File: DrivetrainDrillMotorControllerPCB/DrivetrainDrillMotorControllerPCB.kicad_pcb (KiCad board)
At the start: 4 copper layers, 100 x 100 mm, 39 parts, among them J1 DC-005-5A-2.0, J10 Conn_01x02_Socket, J11 Conn_01x02_Socket, J12 Conn_01x02_Socket, J13 Conn_01x02_Socket, J14 Conn_01x02_Socket, J15 Conn_01x02_Socket, J16 Conn_01x02_Socket, J17 Conn_01x08_Socket, J2 Conn_01x02_Socket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

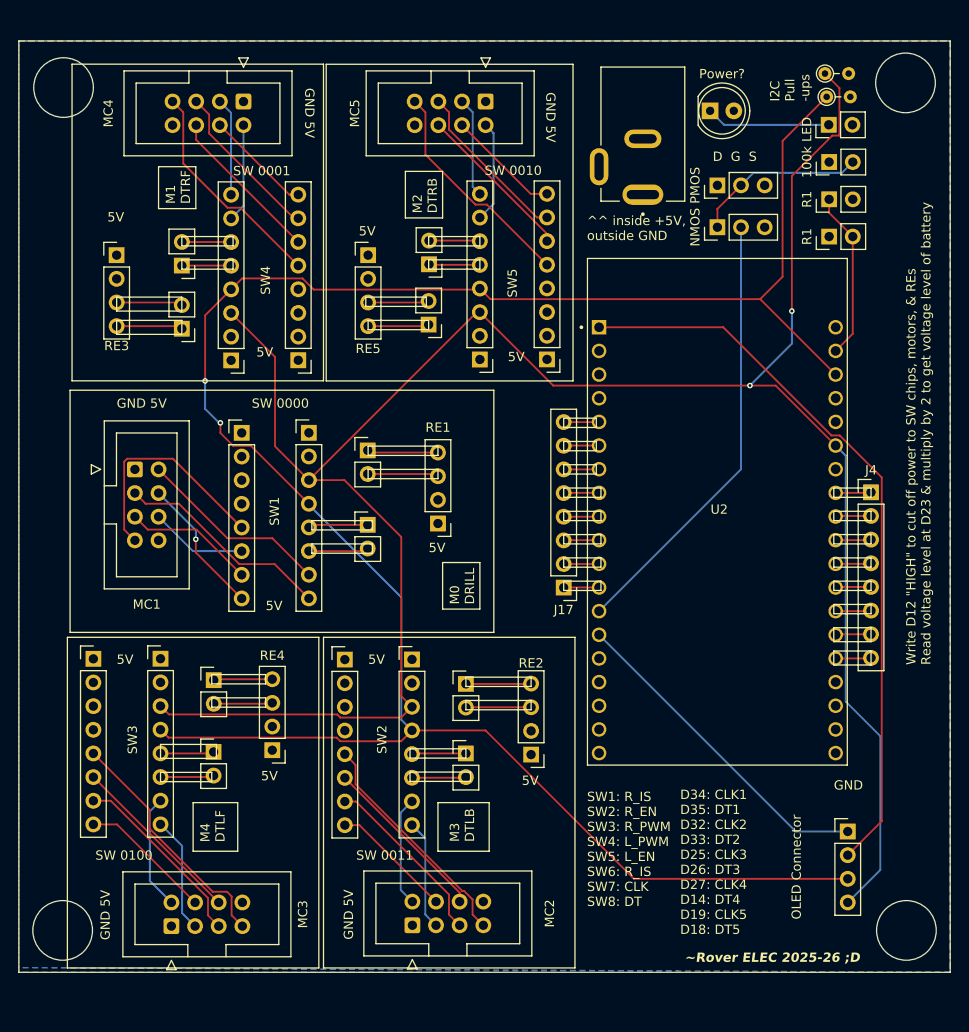
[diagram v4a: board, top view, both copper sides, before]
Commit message: Corrected devkit footprint
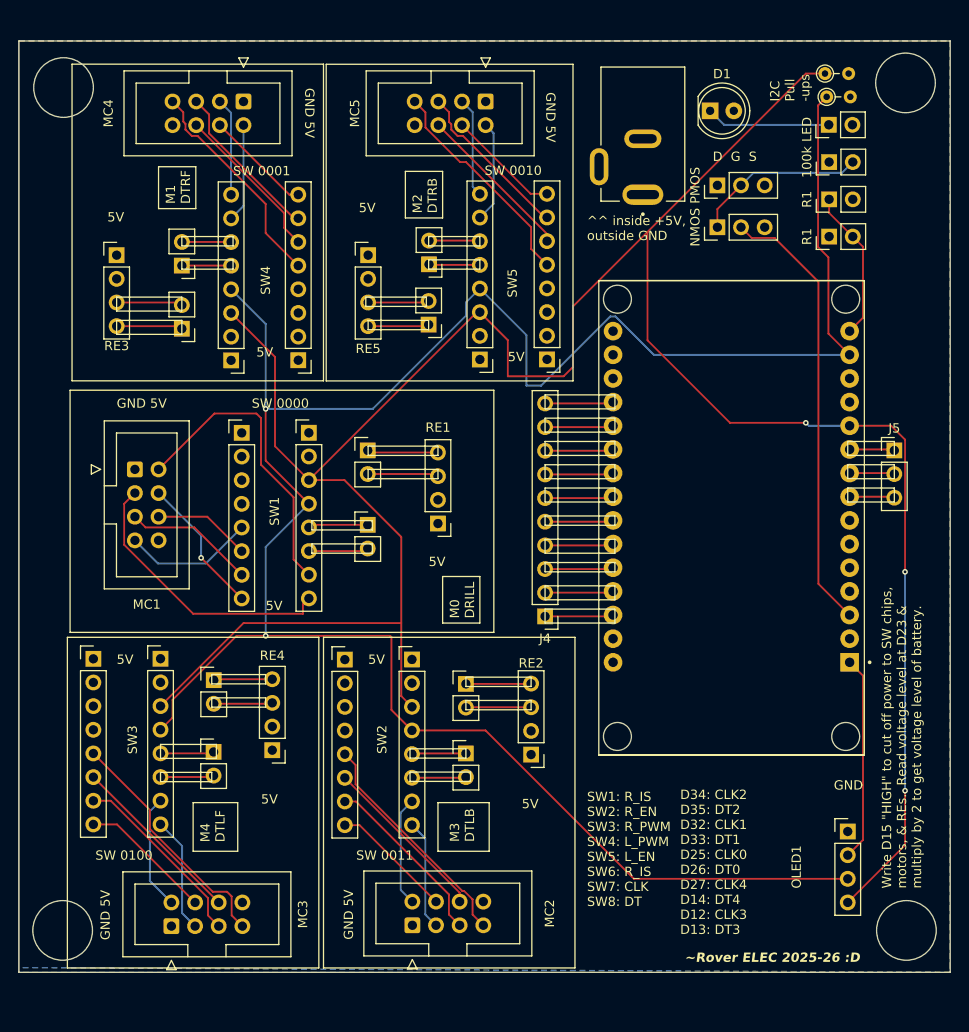
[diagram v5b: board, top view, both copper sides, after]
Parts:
- removed J17: Conn_01x08_Socket, Connector_PinHeader_2.54mm:PinHeader_1x08_P2.54mm_Vertical
- removed U2: ESP32-DEVKITC-32D, ESP32-DEVKITC-32D:MODULE_ESP32-DEVKITC-32D
- added J5: Conn_01x03_Socket, Connector_PinHeader_2.54mm:PinHeader_1x03_P2.54mm_Vertical, F.Cu at (151.5, 104.0)
- added U1: ESP32-DEVKIT-V1, ESP32-DEVKIT-V1:MODULE_ESP32_DEVKIT_V1, F.Cu at (134.0, 111.2)
- J4: value Conn_01x08_Socket -> Conn_01x10_Socket; footprint Connector_PinHeader_2.54mm:PinHeader_1x08_P2.54mm_Vertical -> Connector_PinHeader_2.54mm:PinHeader_1x10_P2.54mm_Vertical
- OLED1: renamed from OLED Connector
- moved J4 37.4 mm to (114.0, 121.8), turned to 180 degrees
- gave numbers to parts that had none: 1
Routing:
- net 3.3V: track 79.1 -> 22.0 mm
- net GND: track 35.4 -> 0.00 mm
- net SDA: track 241.6 -> 264.0 mm, vias 2 -> 3
- net SCL: track 234.7 -> 248.0 mm
- net Net-(MC1-Pin_2): track 20.8 -> 32.6 mm
- net Net-(MC1-Pin_7): track 24.7 -> 14.1 mm
- net Net-(J4-Pin_9): track 0.00 -> 7.36 mm
- net Net-(J4-Pin_10): track 0.00 -> 7.36 mm
- net Net-(MC1-Pin_3): track 23.4 -> 30.2 mm
- net Net-(J5-Pin_3): track 0.00 -> 4.84 mm
- net Net-(J5-Pin_2): track 0.00 -> 4.84 mm
- net Net-(J5-Pin_1): track 0.00 -> 4.84 mm
- net Net-(J17-Pin_5): track 3.81 -> 0.00 mm
- net Net-(J17-Pin_3): track 3.81 -> 0.00 mm
- net Net-(J17-Pin_8): track 3.81 -> 0.00 mm
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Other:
- board text added: "D34: CLK2 D35: DT2 D32: CLK1 D33: DT1 D25: CLK0 D26: DT0 D27: CLK4 D14: DT4 D12: CLK3 D13: DT3"
- board text added: "Write D15 {dblquote}HIGH{dblquote} to cut off power to SW chips, motors, & REs. Read voltage level at D23 & multiply by 2 to get voltage level of battery."
- board text added: "~Rover ELEC 2025-26 :D"
- board text removed: "D34: CLK1 D35: DT1 D32: CLK2 D33: DT2 D25: CLK3 D26: DT3 D27: CLK4 D14: DT4 D19: CLK5 D18: DT5"
- board text removed: "Write D12 {dblquote}HIGH{dblquote} to cut off power to SW chips, motors, & REs Read voltage level at D23 & multiply by 2 to get voltage level of battery"
- board text removed: "~Rover ELEC 2025-26 ;D"

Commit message: made esp32 power from battery optional
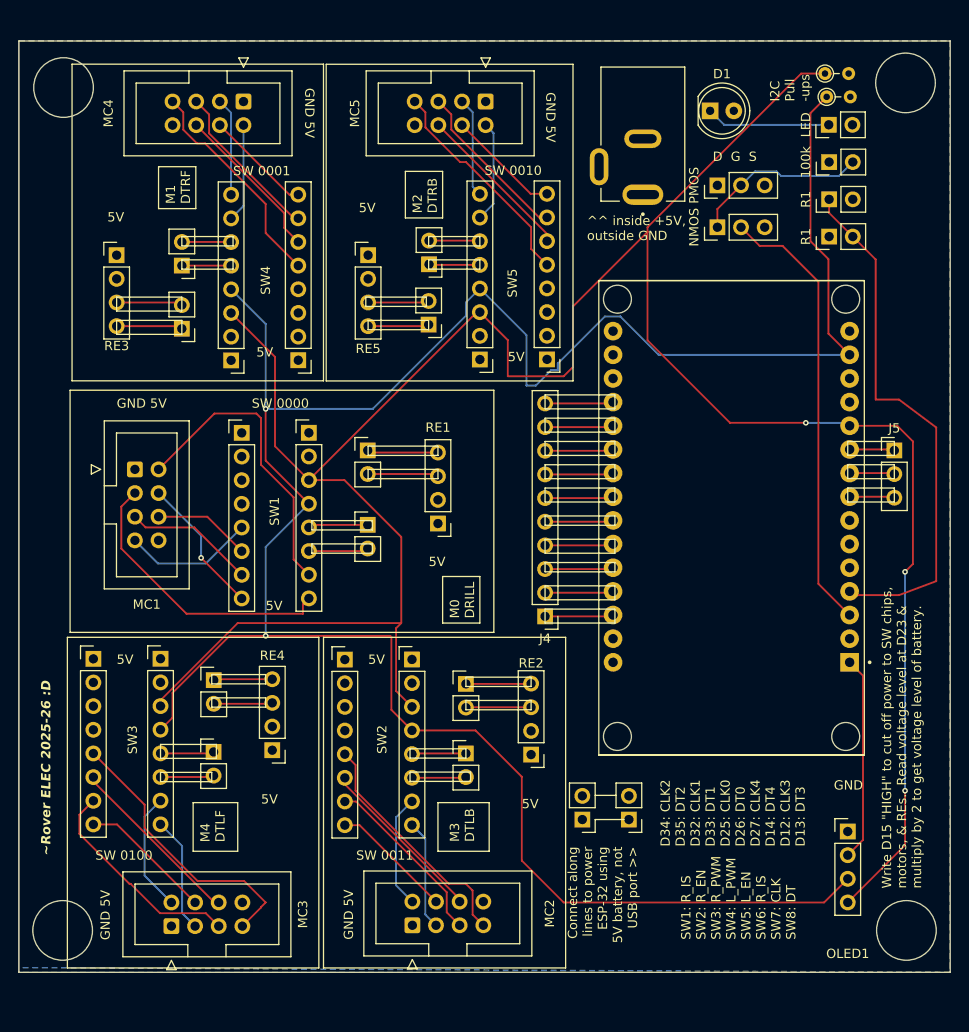
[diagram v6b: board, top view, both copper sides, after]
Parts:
- added J6: Conn_01x02_Socket, Connector_PinHeader_2.54mm:PinHeader_1x02_P2.54mm_Vertical, F.Cu at (123.0, 143.6)
- added J7: Conn_01x02_Socket, Connector_PinHeader_2.54mm:PinHeader_1x02_P2.54mm_Vertical, F.Cu at (118.0, 143.6)
- renumbered 100k to 100k1, PMOS to Q1, NMOS to Q2, R1 to R3, R1 to R4, LED to R5
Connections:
- R3 pad 1: Net-(U1-D23) -> Net-(U1-D2)
- R4 pad 2: Net-(U1-D23) -> Net-(U1-D2)
- U1 pad 15: Net-(U1-D23) -> unconnected-(U1-D23-Pad15)
- U1 pad 30: original5V -> ESP32Feeder
- U1 pad 4: unconnected-(U1-D2-Pad4) -> Net-(U1-D2)
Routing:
- net Net-(U1-D2): track 0.00 -> 23.6 mm
- net Net-(U1-D23): track 16.3 -> 0.00 mm
- net SCL: track 248.0 -> 256.9 mm
- net Net-(MC3-Pin_7): track 26.1 -> 30.2 mm
- net Net-(MC3-Pin_5): track 20.1 -> 23.2 mm
- net SDA: track 264.0 -> 266.3 mm
- net Net-(MC2-Pin_7): track 24.6 -> 25.6 mm
- net Net-(MC1-Pin_3): track 30.2 -> 30.9 mm
- added copper zone on In2.Cu, net ESP32Feeder
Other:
- board text added: "100k"
- board text added: "Connect along lines to power ESP-32 using 5V battery, not USB port >>"
- board text added: "LED"
- board text added: "NMOS"
- board text added: "PMOS"
- board text added: "R1"

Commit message: Added linear regulator
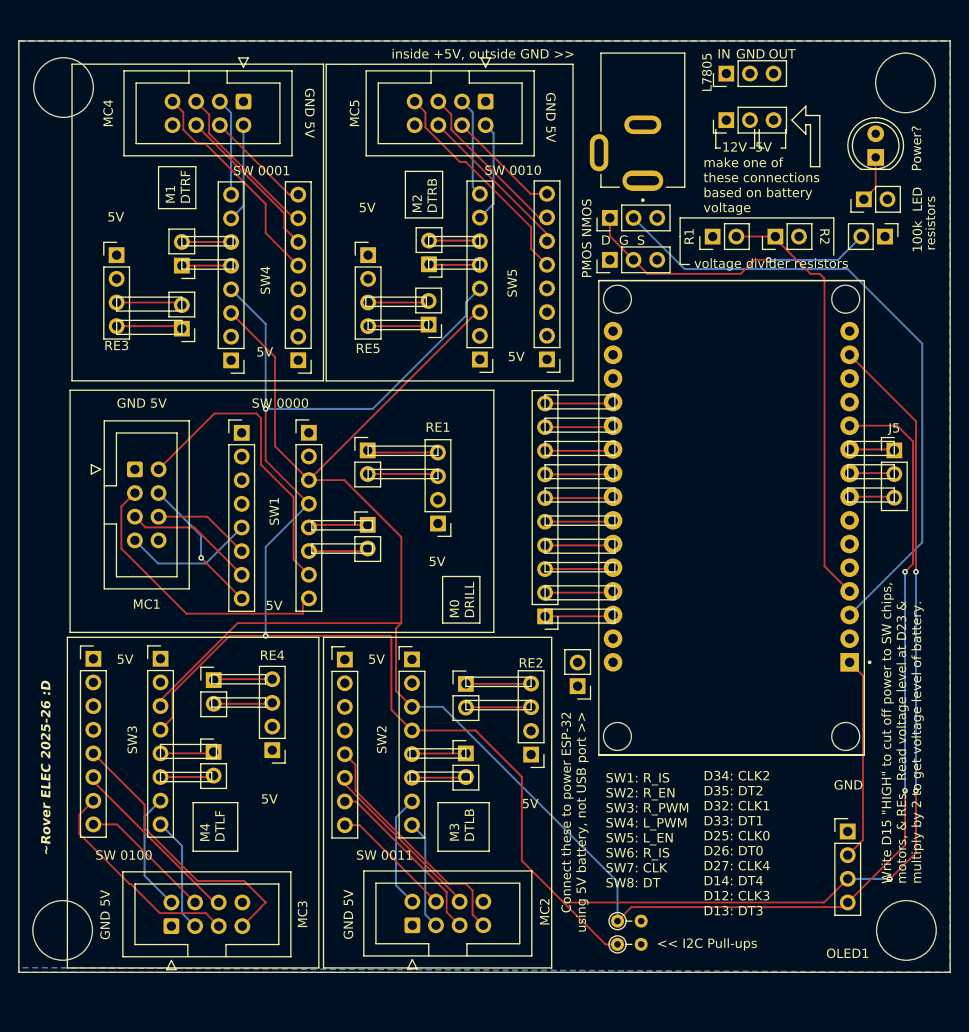
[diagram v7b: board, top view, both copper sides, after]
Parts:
- added U3: L7805, Connector_PinHeader_2.54mm:PinHeader_1x03_P2.54mm_Vertical, F.Cu at (133.5, 63.5)
- J7: value Conn_01x02_Socket -> Conn_01x03_Pin; footprint Connector_PinHeader_2.54mm:PinHeader_1x02_P2.54mm_Vertical -> Connector_PinHeader_2.54mm:PinHeader_1x03_P2.54mm_Vertical
- moved R1 93.7 mm to (121.8, 157.0)
- moved R2 93.7 mm to (121.8, 154.5)
- moved J7 76.7 mm to (133.5, 68.5), turned to 90 degrees
- moved D1 18.5 mm to (149.5, 72.5), turned to 90 degrees
- moved J6 15.3 mm to (117.5, 129.3)
- moved Q1 14.0 mm to (121.0, 83.5)
- moved R4 12.5 mm to (132.0, 81.0)
- moved Q2 11.6 mm to (121.0, 79.0)
- moved 100k1 10.0 mm to (150.5, 81.0), turned to -90 degrees
- moved R5 8.84 mm to (148.2, 77.0)
- moved R3 7.03 mm to (138.7, 81.0)
- moved J1 1.50 mm to (124.5, 69.0)
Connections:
- J1 pad 1: original5V -> Vin
- J6 pad 2: original5V -> ESP32Feeder
- J7 pad 1: ESP32Feeder -> Net-(J7-Pin_1)
- J7 pad 2: ESP32Feeder -> Vin
- R4 pad 1: original5V -> Vin
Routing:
- net SDA: track 266.3 -> 228.7 mm, vias 3 -> 2
- net Net-(U1-D2): track 23.6 -> 46.2 mm
- net Net-(Q2-G): track 47.9 -> 69.0 mm
- net Net-(Q1-G): track 19.0 -> 32.3 mm, vias 0 -> 1
- net SCL: track 256.9 -> 246.9 mm, vias 2 -> 6
- net Net-(D1-K): track 13.4 -> 5.03 mm
- net Net-(J7-Pin_1): track 0.00 -> 5.00 mm
- added copper zone on In2.Cu, net Vin
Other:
- board text added: "12V 5V"
- board text added: "<< I2C Pull-ups"
- board text added: "Connect these to power ESP-32 using 5V battery, not USB port >>"
- board text added: "IN"
- board text added: "L7805"
- board text added: "OUT"
- board text added: "Power?"
- board text added: "R2"
- board text added: "inside +5V, outside GND >>"
- board text added: "make one of these connections based on battery voltage"
- board text added: "resistors"
- board text added: "voltage divider resistors"
- board text removed: "Connect along lines to power ESP-32 using 5V battery, not USB port >>"
- board text removed: "I2C Pull -ups"
- board text removed: "^^ inside +5V, outside GND"
